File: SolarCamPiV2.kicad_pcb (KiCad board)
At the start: 4 copper layers, 65 x 30 mm, 95 parts, among them J1 TagConnect_TC2030_SWD, J2 RPi, J3 FTDI_RPI, Q1 AO3401A, Q2 AO3401A, Q3 2N7002, Q4 AO3401A, Q5 2N7002, Q6 BSS84, SW1 User, U1 CN3767, U2 HT7533, U3 SY8113B, U4 STM32G031Fx, Y1 32.768kHz

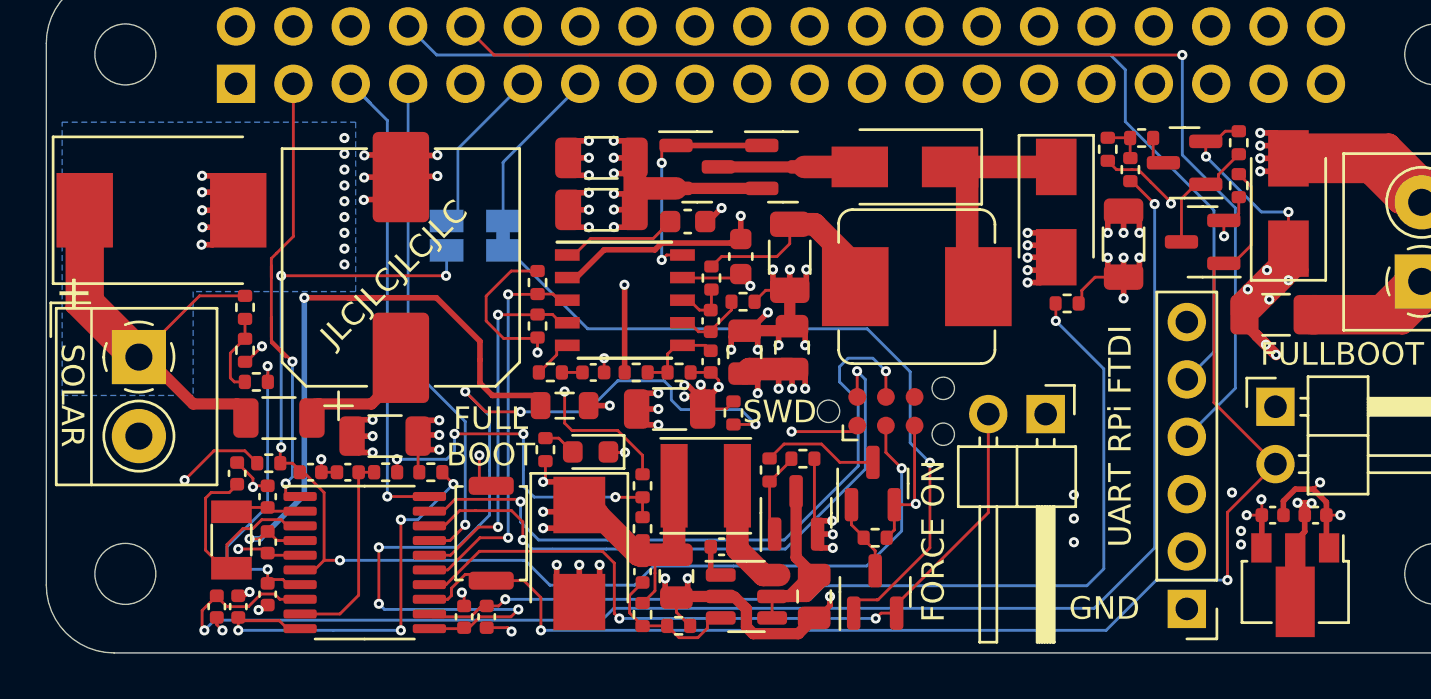
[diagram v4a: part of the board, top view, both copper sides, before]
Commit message: DFM, add pin 1 designators
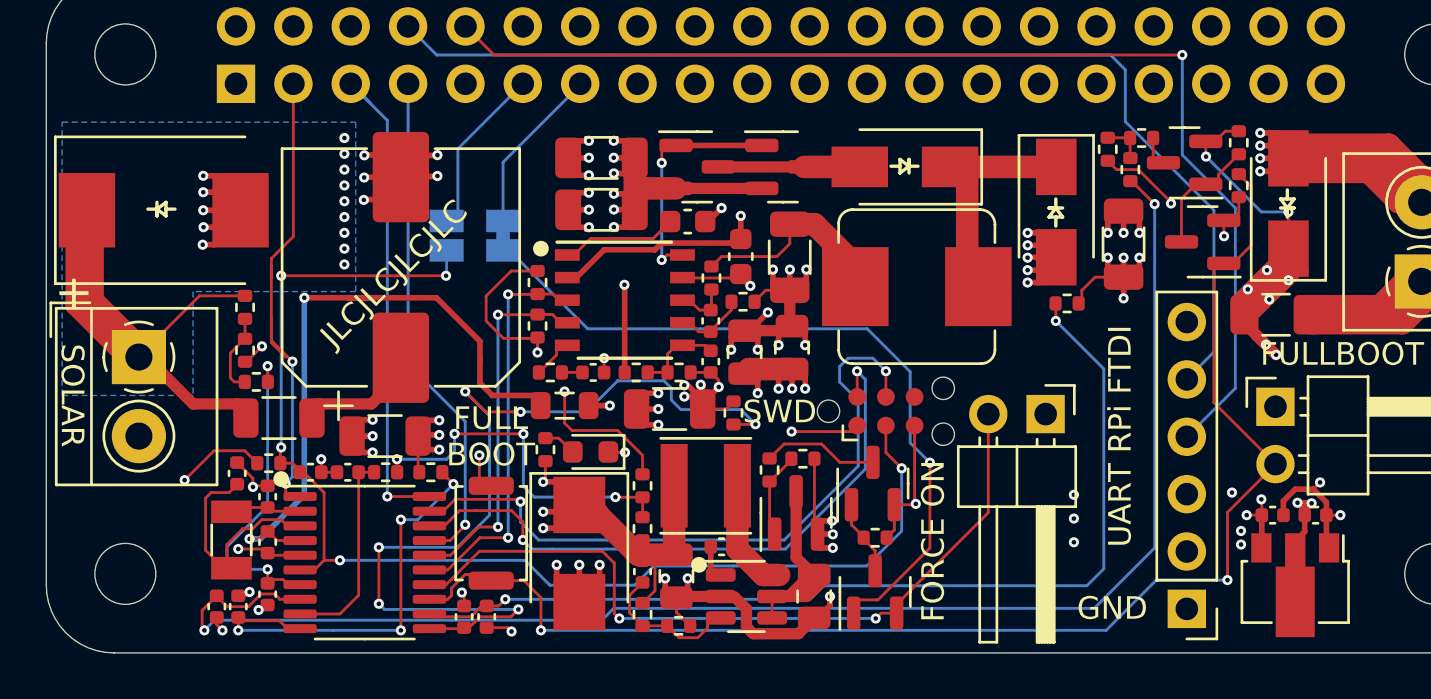
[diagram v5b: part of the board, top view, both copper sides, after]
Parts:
- moved D6 0.10 mm to (105.2, 110.4)
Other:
- board text added: "MPPT Solar Cam Pi V2 Rev 1.0 Designed by Tobias Schramm in 2022"
- board text removed: "Solar Cam Pi V2 Rev 1.0 Designed by Tobias Schramm in 2022"

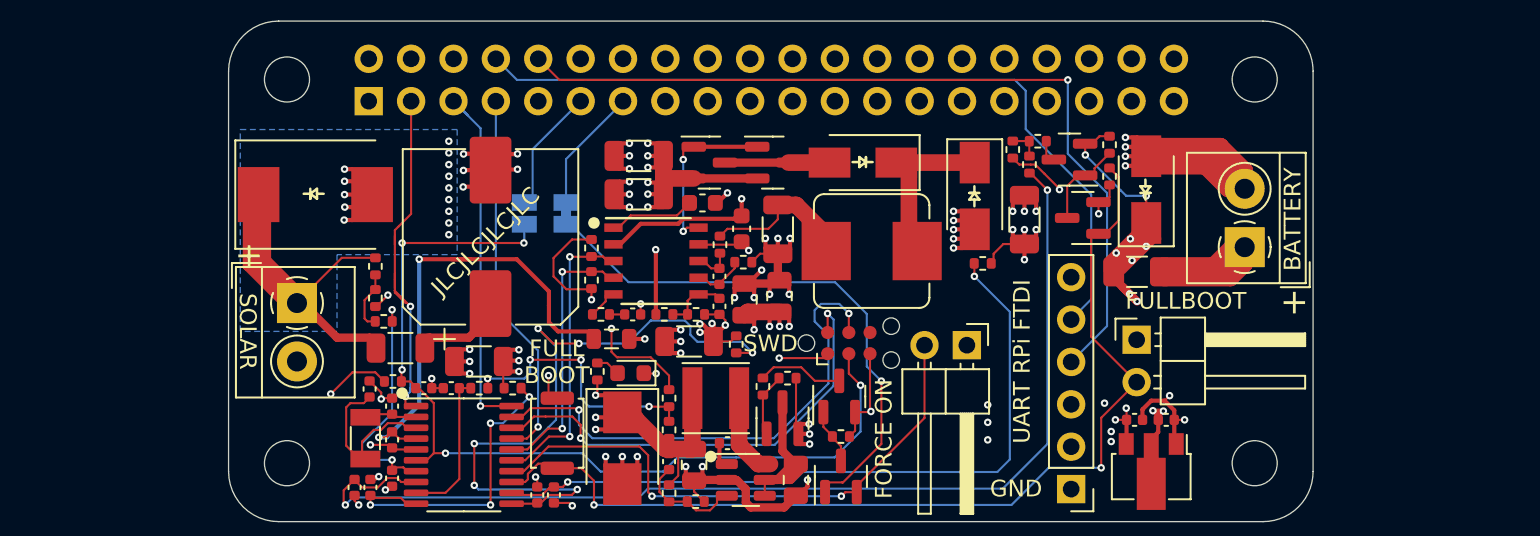
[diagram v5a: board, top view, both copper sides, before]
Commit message: Connect SWD to RPi GPIOs
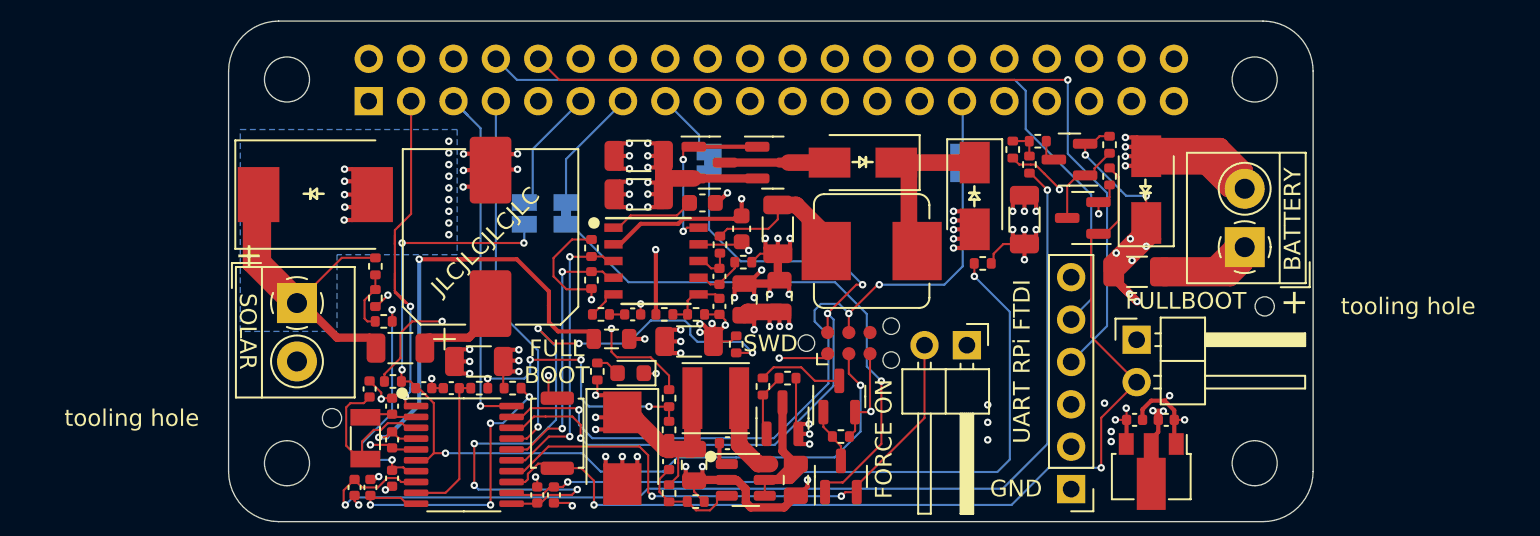
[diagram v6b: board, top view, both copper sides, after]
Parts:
- added H5: ToolingHole, ToolingHole:ToolingHole_JLCSMT, F.Cu at (106.2, 123.8)
- added H6: ToolingHole, ToolingHole:ToolingHole_JLCSMT, F.Cu at (162.1, 117.1)
- added JP5: SWCLK, Jumper:SolderJumper-2_P1.3mm_Bridged_Pad1.0x1.5mm, B.Cu at (144.0, 108.5)
- added JP6: SWDIO, Jumper:SolderJumper-2_P1.3mm_Bridged_Pad1.0x1.5mm, B.Cu at (128.8, 108.5)
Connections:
- J2 pad 15: unconnected-(J2-Pad15) -> Net-(J2-Pad15)
- J2 pad 29: unconnected-(J2-Pad29) -> Net-(J2-Pad29)
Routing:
- net /SWDIO: track 27.8 -> 44.6 mm, vias 2 -> 3
- net /SWCLK: track 30.2 -> 43.7 mm, vias 2 -> 3
- net Net-(J2-Pad15): track 0.00 -> 3.64 mm
- net Net-(J2-Pad29): track 0.00 -> 3.05 mm
- net +3V3: track 19.6 -> 21.7 mm
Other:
- board text added: "SWCLK"
- board text added: "SWDIO"
